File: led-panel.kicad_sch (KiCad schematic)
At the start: 12 parts

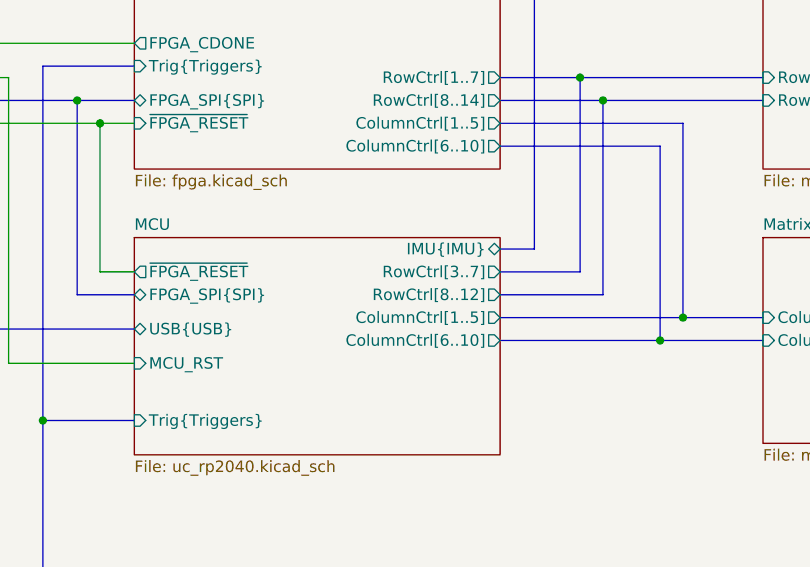
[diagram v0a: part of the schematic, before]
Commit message: [#72533] PCB: routing complete
Signed-off-by: Dawid Lentka <dlentka@antmicro.com>
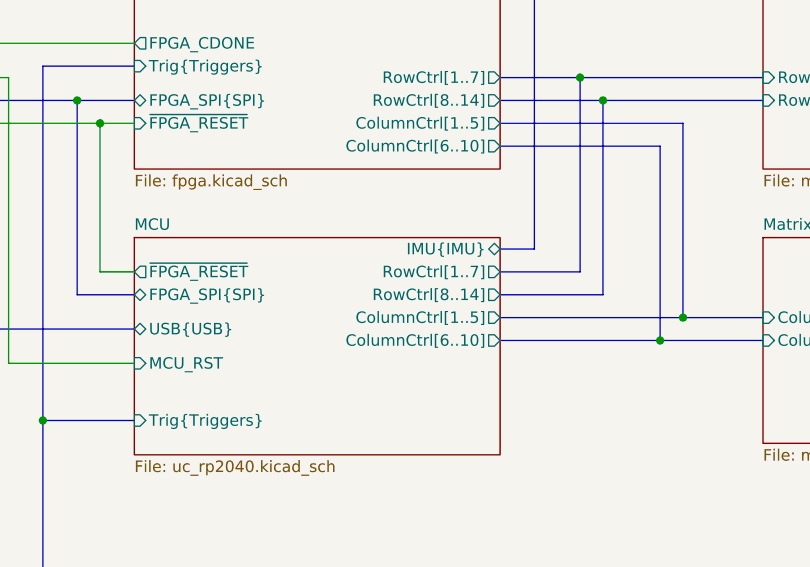
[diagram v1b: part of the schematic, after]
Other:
- sheet MCU ports: added RowCtrl[1..7], RowCtrl[8..14]; removed RowCtrl[3..7], RowCtrl[8..12]
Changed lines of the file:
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@@
 			)
 		)
-		(pin "RowCtrl[3..7]" output
+		(pin "RowCtrl[1..7]" output
 			(at 132.08 101.6 0)
 			(effects
@@
 			)
 		)
-		(pin "RowCtrl[8..12]" output
+		(pin "RowCtrl[8..14]" output
 			(at 132.08 104.14 0)
 			(effects
